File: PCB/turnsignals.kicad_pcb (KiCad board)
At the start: 2 copper layers, 31.5 x 34.1 mm, 22 parts

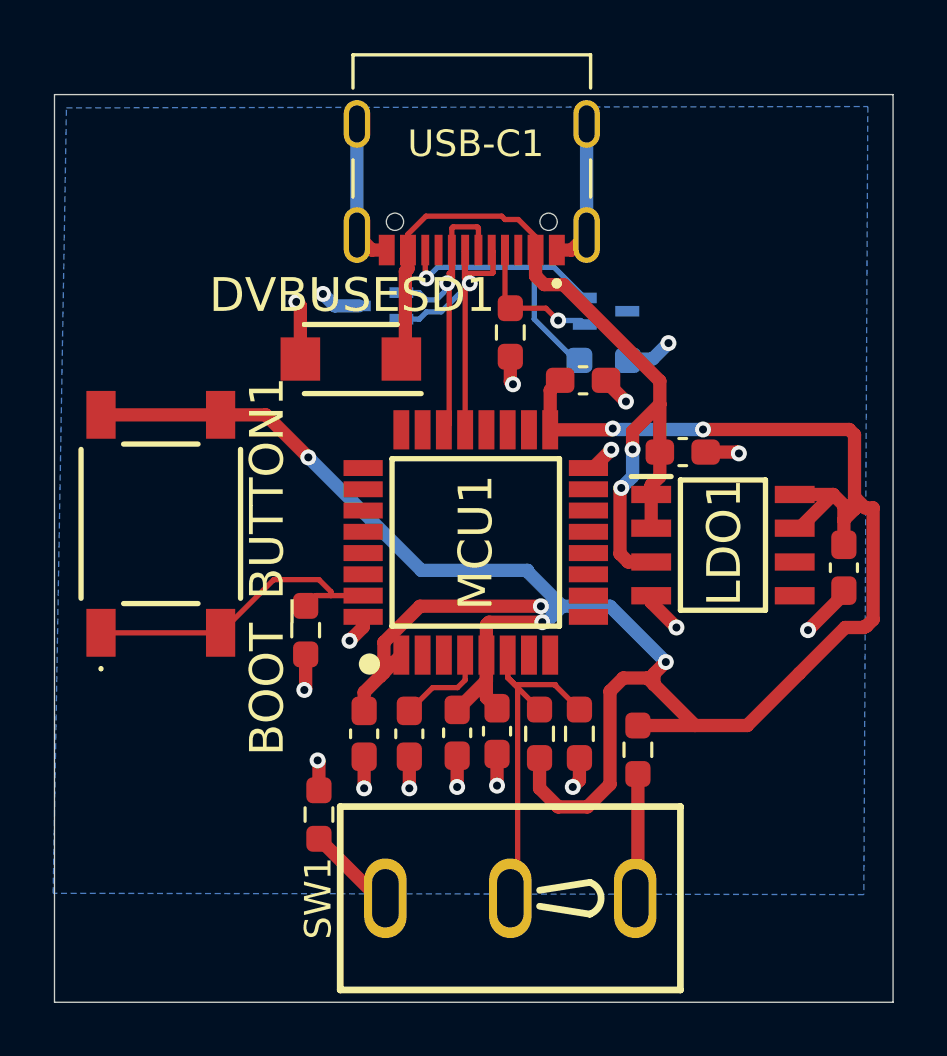
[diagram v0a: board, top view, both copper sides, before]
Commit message: Corrected button wiring
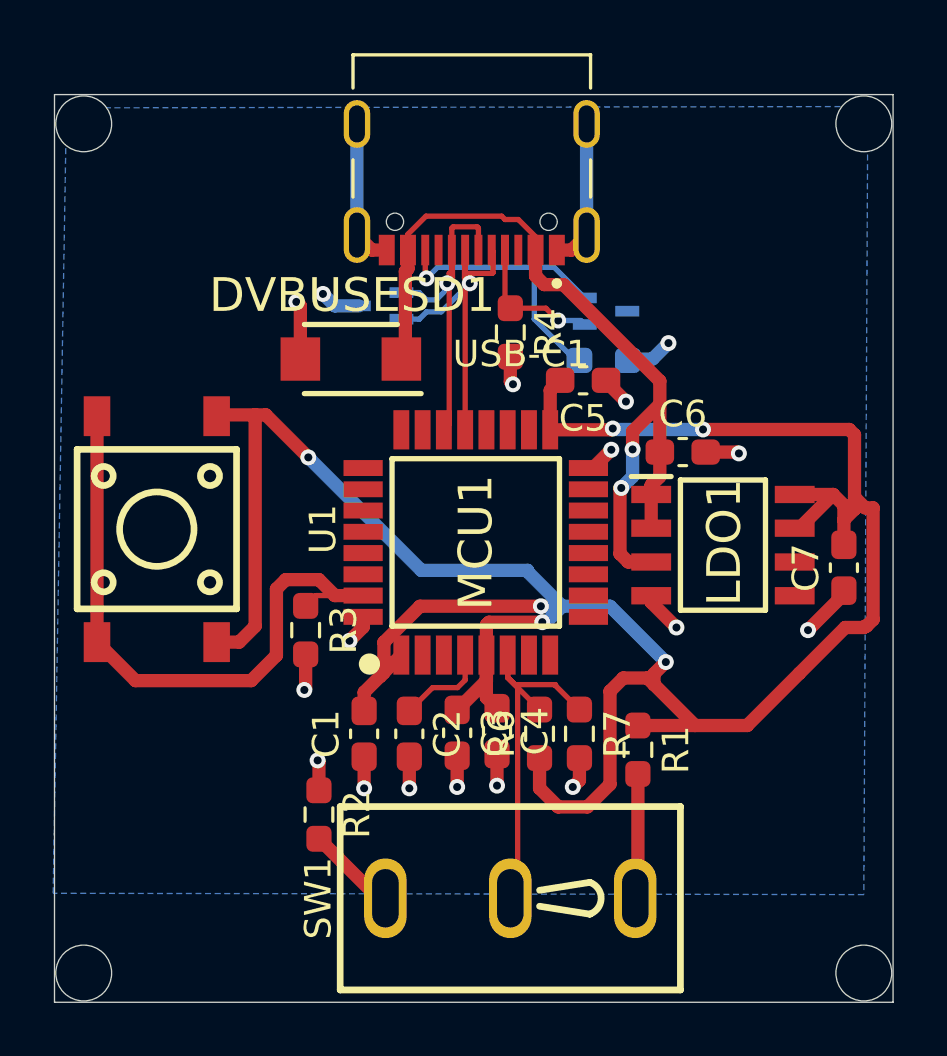
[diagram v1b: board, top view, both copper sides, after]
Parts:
- removed BOOT_BUTTON1: SHOU HAN TS6643TP 250gf 009, REQUIRED:TS406643BK160SMTTR
- added ?: , REQUIRED:, F.Cu at (126.0, 63.8)
- added ?: , REQUIRED:, F.Cu at (155.4, 63.8)
- added ?: , REQUIRED:, F.Cu at (126.0, 95.7)
- added ?: , REQUIRED:, F.Cu at (155.4, 95.7)
- added U1: TS6643TP 250GF 009, REQUIRED:SW-SMD_4P-L6.2-W6.0-P4.50-LS9.0, F.Cu at (128.8, 79.0)
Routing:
- net Net-(MCU1-PB8-BOOT0): track 12.1 -> 24.7 mm
- net +3.3V: track 96.5 -> 101.6 mm
